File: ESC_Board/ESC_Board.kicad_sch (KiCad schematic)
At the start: 0 parts

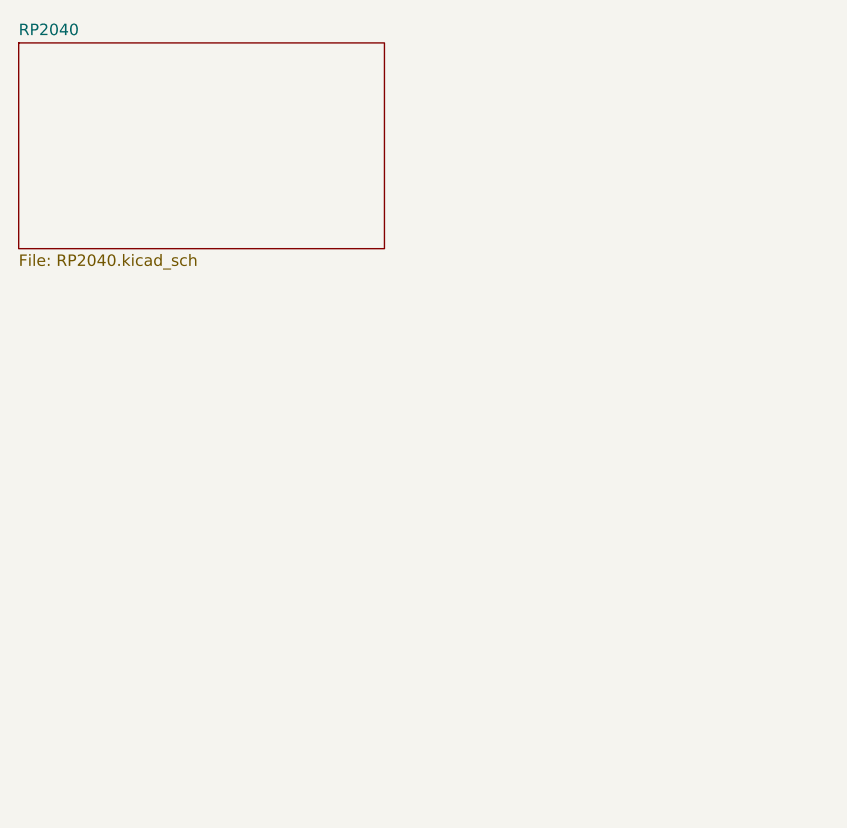
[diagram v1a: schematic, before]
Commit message: added esc interface pageand added test points to the rp2040 page
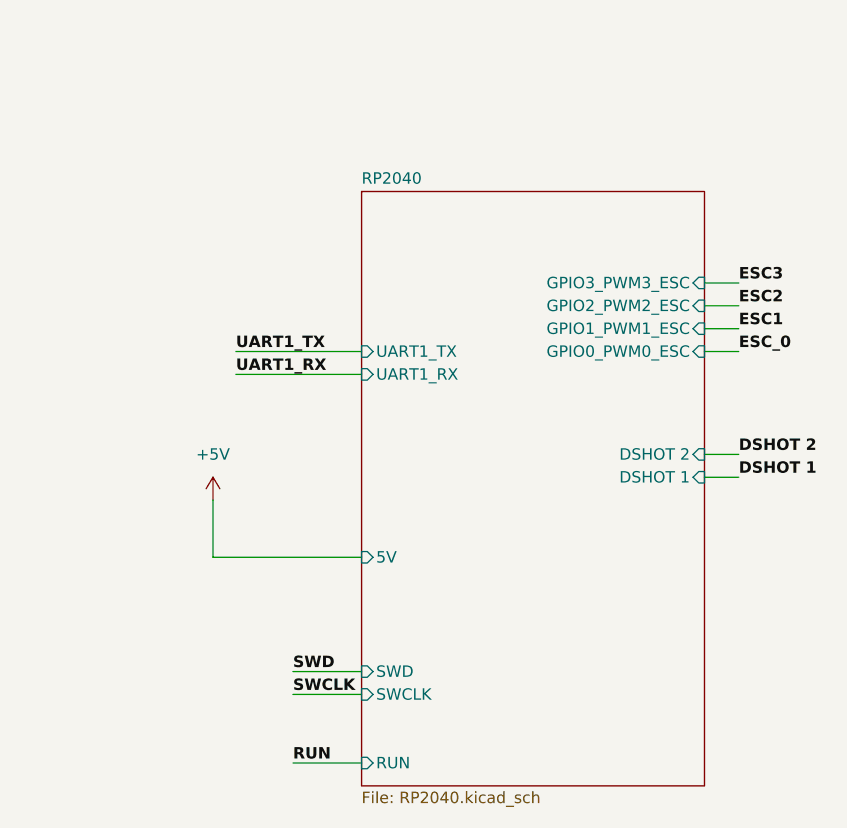
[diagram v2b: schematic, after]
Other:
- sheet RP2040 ports: added 5V, DSHOT 1, DSHOT 2, GPIO0_PWM0_ESC, GPIO1_PWM1_ESC, GPIO2_PWM2_ESC, GPIO3_PWM3_ESC, RUN, SWCLK, SWD, UART1_RX, UART1_TX; removed none

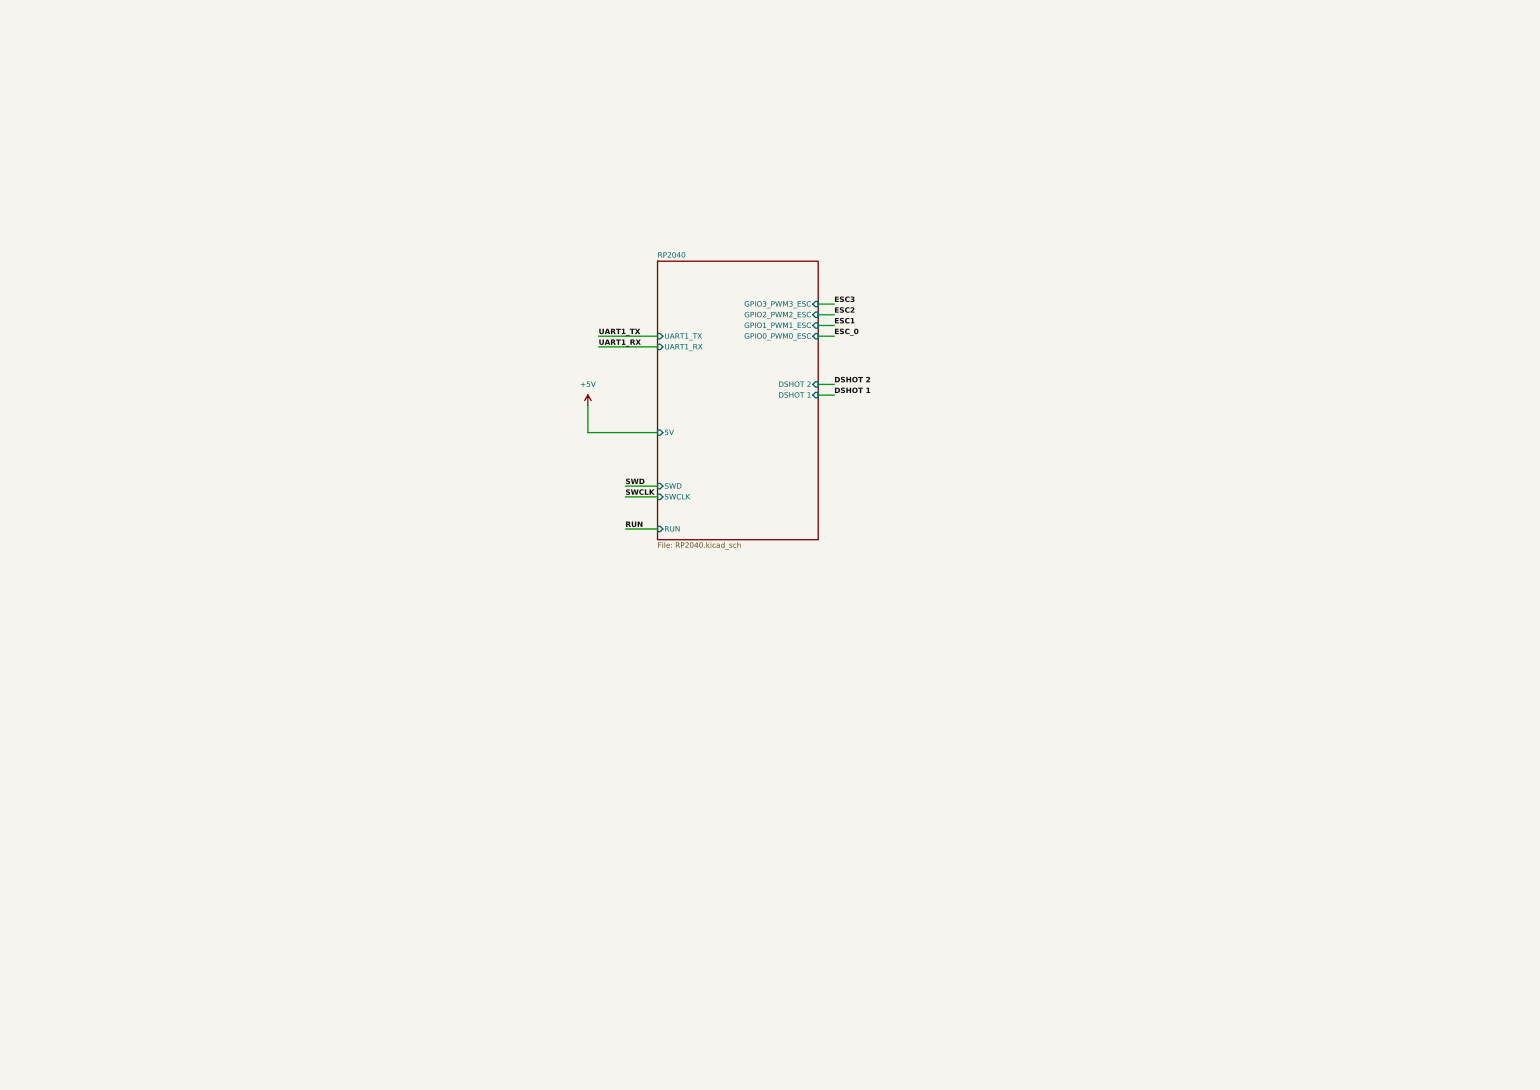
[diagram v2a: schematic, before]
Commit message: schematic done, ready for review. need to think about how this will connect to the backplane
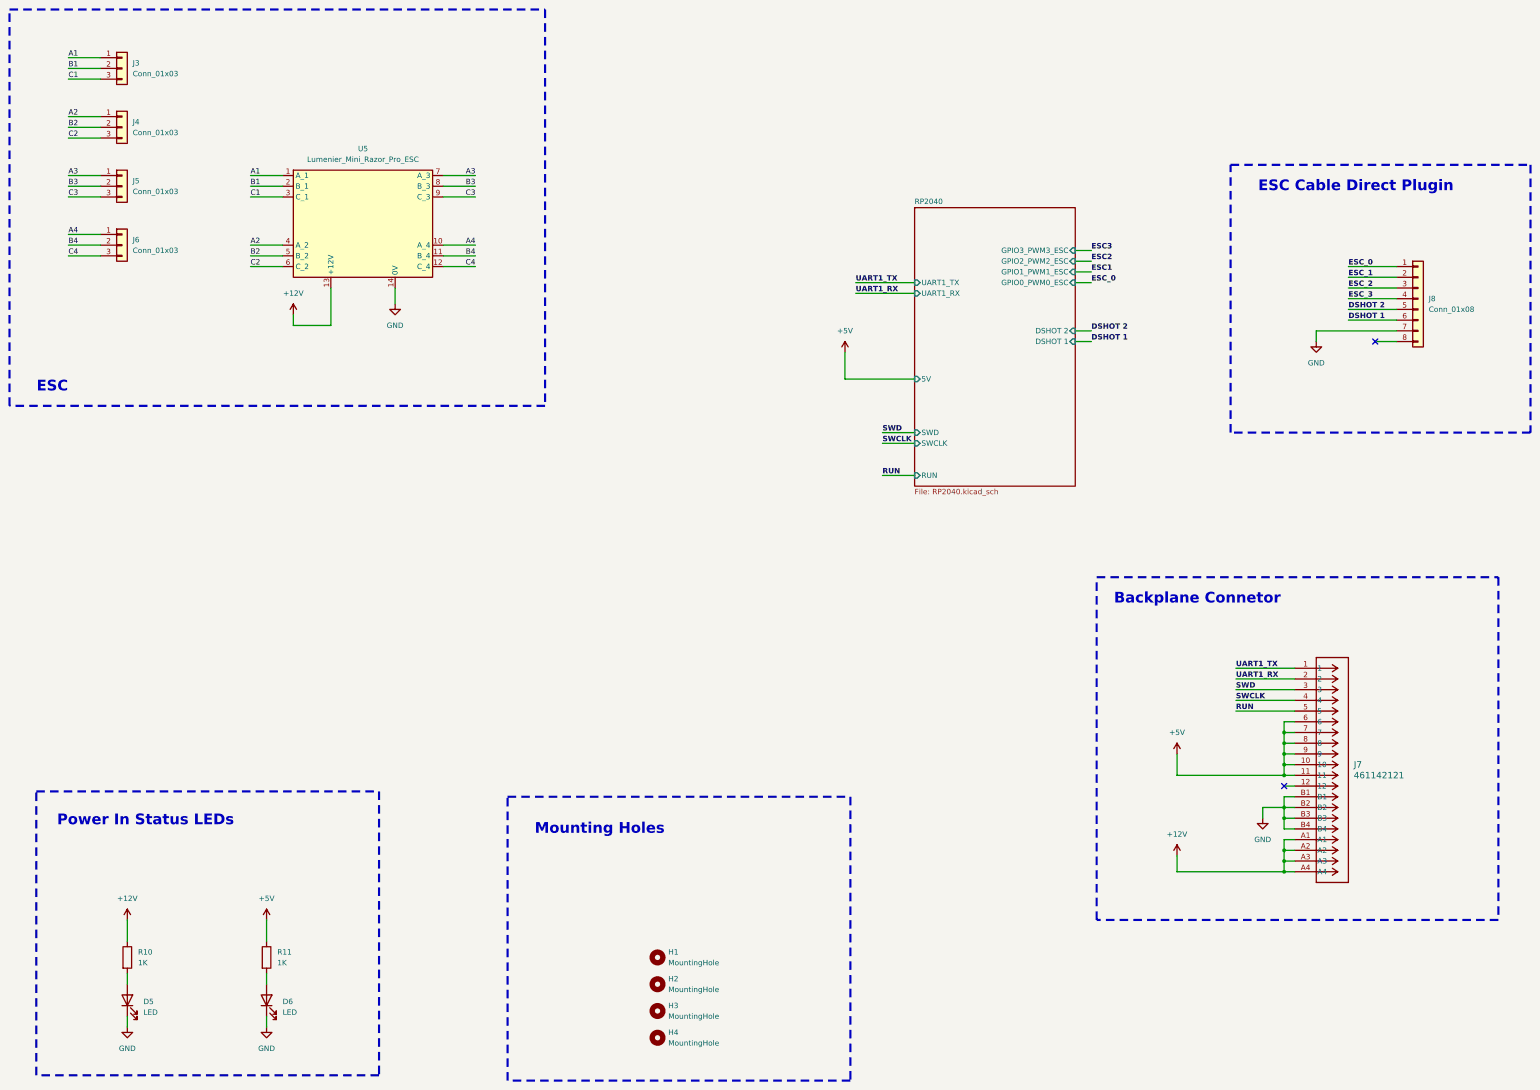
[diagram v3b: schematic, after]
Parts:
- added D5, D6: LED, symbol Device:LED
- added H1, H2, H3, H4: MountingHole, symbol Mechanical:MountingHole
- added J3, J4, J5, J6: Conn_01x03, symbol Connector_Generic:Conn_01x03
- added J7: 461142121, CON_461142121, symbol molex_2024-08-21:461142121
- added J8: Conn_01x08, symbol Connector_Generic:Conn_01x08
- added R10, R11: 1K, symbol Device:R
- added U5: Lumenier_Mini_Razor_Pro_ESC, symbol Lumenier_Mini_Razor_Pro_ESC:Lumenier_Mini_Razor_Pro_ESC
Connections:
- net +5V: now also J7.10, J7.11, J7.6, J7.7, J7.8, J7.9, R11.1
- net DSHOT 1: now also J8.6 (Pin_6)
- net DSHOT 2: now also J8.5 (Pin_5)
- net ESC_0: now also J8.1 (Pin_1)
- net RUN: now also J7.5
- net SWCLK: now also J7.4
- net SWD: now also J7.3
- net UART1_RX: now also J7.2
- net UART1_TX: now also J7.1
- new net: D6.2 (A), R11.2
- new net: D5.2 (A), R10.2
- new net +12V: J7.A1, J7.A2, J7.A3, J7.A4, R10.1, U5.13 (+12V)
- new net A1: J3.1 (Pin_1), U5.1 (A_1)
- new net A2: J4.1 (Pin_1), U5.4 (A_2)
- new net A3: J5.1 (Pin_1), U5.7 (A_3)
- new net A4: J6.1 (Pin_1), U5.10 (A_4)
- new net B1: J3.2 (Pin_2), U5.2 (B_1)
- new net B2: J4.2 (Pin_2), U5.5 (B_2)
- new net B3: J5.2 (Pin_2), U5.8 (B_3)
- new net B4: J6.2 (Pin_2), U5.11 (B_4)
- new net C1: J3.3 (Pin_3), U5.3 (C_1)
- new net C2: J4.3 (Pin_3), U5.6 (C_2)
- new net C3: J5.3 (Pin_3), U5.9 (C_3)
- new net C4: J6.3 (Pin_3), U5.12 (C_4)
- new net ESC_1: J8.2 (Pin_2)
- new net ESC_2: J8.3 (Pin_3)
- new net ESC_3: J8.4 (Pin_4)
- new net GND: D5.1 (K), D6.1 (K), J7.B1, J7.B2, J7.B3, J7.B4, J8.7 (Pin_7), U5.14 (0V)
- no-connect marks 0 -> 2
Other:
- note added: "Backplane Connetor"
- note added: "ESC"
- note added: "ESC Cable Direct Plugin"
- note added: "Mounting Holes"
- note added: "Power In Status LEDs"

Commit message: esc board updated
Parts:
- removed J7: 461142121, CON_461142121, symbol molex_2024-08-21:461142121
- added J9: IPS1-120-01-L-D, IPS1-120-01-L-D:SAMTEC_IPS1-120-01-L-D, symbol IPS1-120-01-L-D:IPS1-120-01-L-D
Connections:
- net +12V: now also J9.21, J9.23, J9.25, J9.27, J9.29, J9.31, J9.33, J9.35, J9.37, J9.39
- net +5V: now also J9.19, J9.20
- net GND: now also J9.01, J9.02, J9.06, J9.07, J9.08, J9.10, J9.12, J9.13, J9.14, J9.15, J9.16, J9.17, J9.18, J9.22, J9.24, J9.26, J9.28, J9.30, J9.32, J9.34, J9.36, J9.38, J9.40
- net RUN: now also J9.04
- net SWCLK: now also J9.11
- net SWD: now also J9.09
- net UART1_RX: now also J9.05
- net UART1_TX: now also J9.03
- no-connect marks 2 -> 1
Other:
- sheet RP2040 ports: added GPIO0, GPIO1, GPIO2, GPIO3; removed GPIO0_PWM0_ESC, GPIO1_PWM1_ESC, GPIO2_PWM2_ESC, GPIO3_PWM3_ESC
- note added: "Each terminal rated for 4.8A"
- note added: "Power On Status LEDs"
- note removed: "Power In Status LEDs"
- company: (none) -> Cabrillo Robotics
- title: (none) -> ESC Board connection
